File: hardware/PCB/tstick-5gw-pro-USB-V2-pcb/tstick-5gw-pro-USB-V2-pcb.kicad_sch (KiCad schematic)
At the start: 66 parts, among them J1 USB_C_Receptacle_USB2.0, Q1 BSS138, Q2 BSS138, Q3 BSS138, SW1 B3U-1000P, SW2 B3U-1000P, U1 USBLC6-2P6, U2 MCP73871, U3 NCP167AMX330TBG, U4 NCP167AMX180TBG

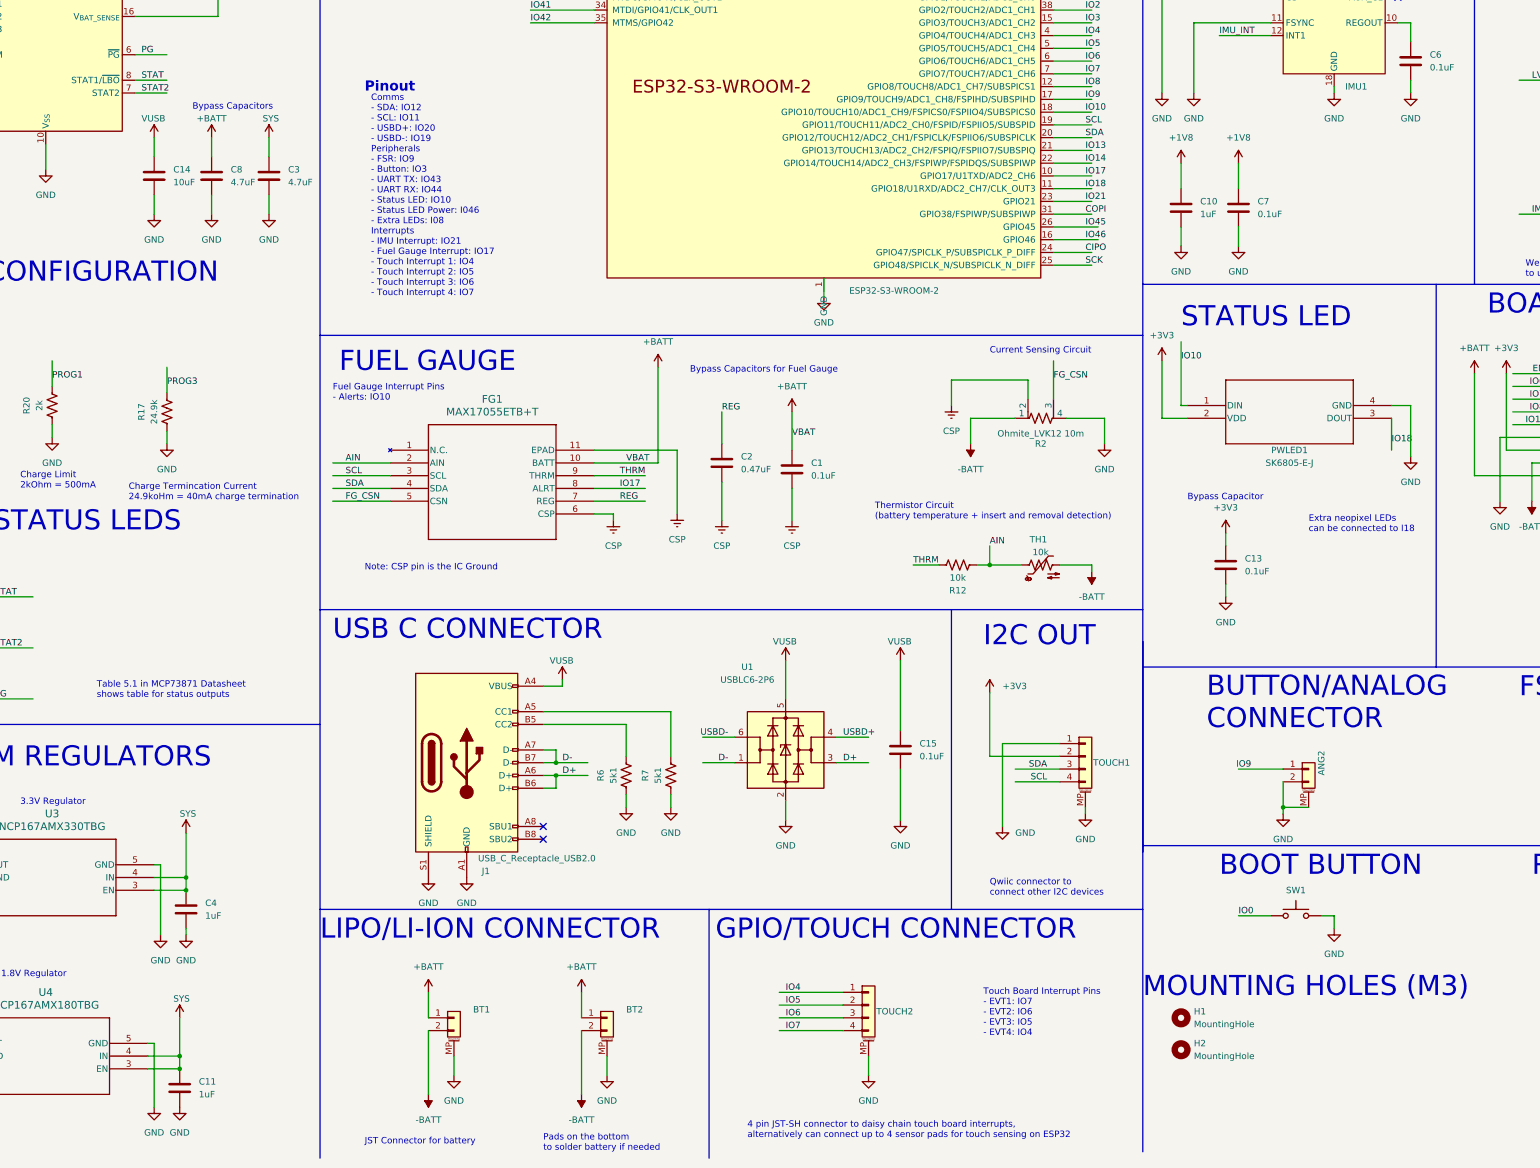
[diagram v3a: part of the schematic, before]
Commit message: removed neopixel, changed BOM, added simple status LEDs
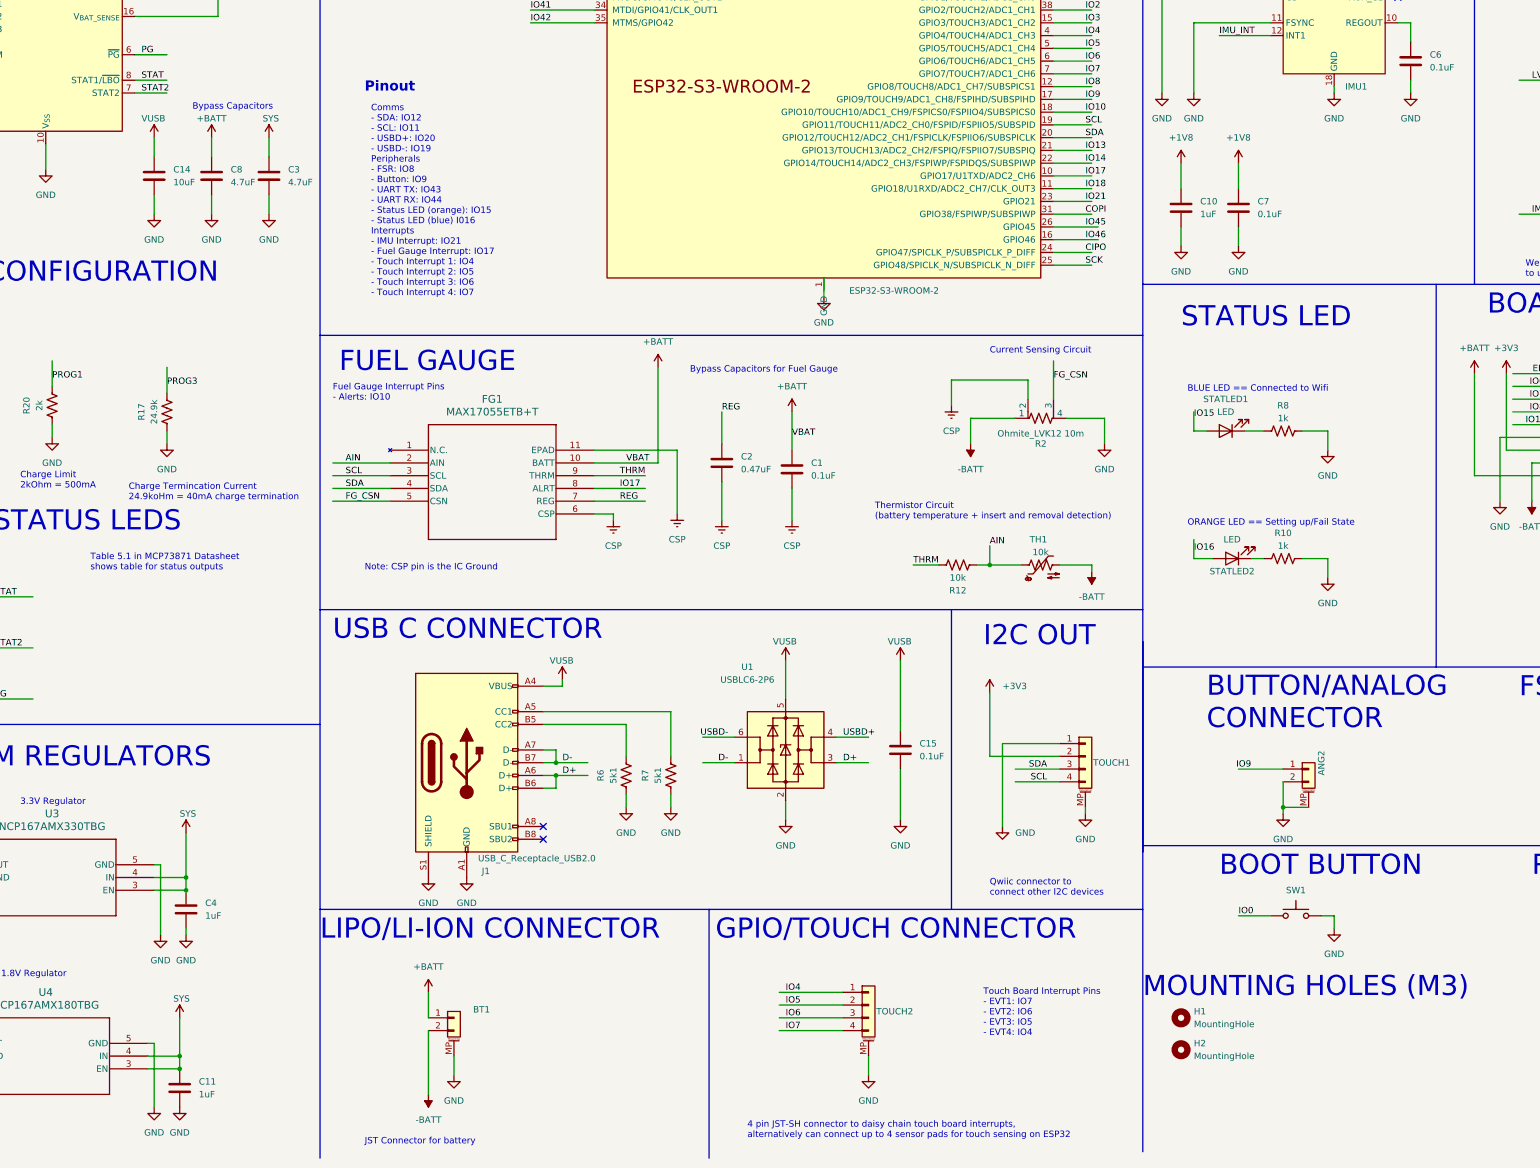
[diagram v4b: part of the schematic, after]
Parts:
- removed BT2: JST-PH-1x02-2.000mm, Connector_JST:JST_PH_B2B-PH-SM4-TB_1x02-1MP_P2.00mm_Vertical, symbol Connector_Generic_MountingPin:Conn_01x02_MountingPin
- removed C13: 0.1uF, Capacitor_SMD:C_0201_0603Metric, symbol Device:C
- removed PWLED1: SK6805-E-J, neopixel-1515-footprints:4492_ADA, symbol neopixel-1515:4492
- added R10, R8: 1k, Resistor_SMD:R_0201_0603Metric, symbol Device:R_US
- added STATLED1, STATLED2: LED, LED_SMD:LED_0402_1005Metric, symbol Device:LED
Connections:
- net GND: now also R10.2, R8.2
- net IO15: now also STATLED1.2 (A)
- net IO16: now also STATLED2.2 (A)
- new net: R8.1, STATLED1.1 (K)
- new net: R10.1, STATLED2.1 (K)
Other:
- note added: "BLUE LED == Connected to Wifi"
- note added: "Comms - SDA: IO12 - SCL: IO11 - USBD+: IO20 - USBD-: IO19 Peripherals - FSR: IO8 - Button: IO9 - UART TX: IO43 - UART RX: IO44 - Status LED (orange): IO15 - Status LED (blue) I016 Interrupts - IMU Interrupt: IO21 - Fuel Gauge Interrupt: IO17 - Touch Interrupt 1: IO4 - Touch Interrupt 2: IO5 - Touch Interrupt 3: IO6 - Touch Interrupt 4: IO7"
- note added: "ORANGE LED == Setting up/Fail State"
- note removed: "Bypass Capacitor"
- note removed: "Comms - SDA: IO12 - SCL: IO11 - USBD+: IO20 - USBD-: IO19 Peripherals - FSR: IO9 - Button: IO3 - UART TX: IO43 - UART RX: IO44 - Status LED: IO10 - Status LED Power: I046 - Extra LEDs: I08 Interrupts - IMU Interrupt: IO21 - Fuel Gauge Interrupt: IO17 - Touch Interrupt 1: IO4 - Touch Interrupt 2: IO5 - Touch Interrupt 3: IO6 - Touch Interrupt 4: IO7"
- note removed: "Extra neopixel LEDs can be connected to I18"
- note removed: "Pads on the bottom to solder battery if needed"

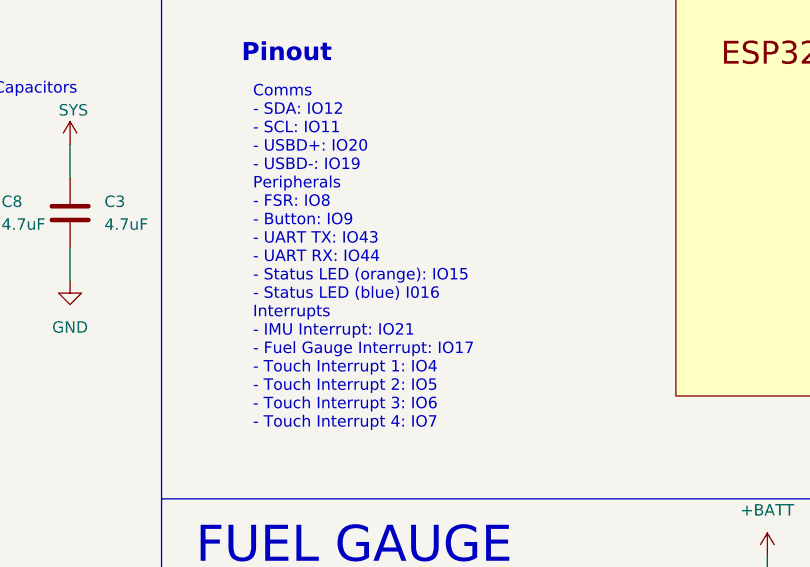
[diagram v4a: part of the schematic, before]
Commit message: Only sends OSC over 1 IP address by default, added class for accessing touch data from custom touch board, uses similar syntax to trill touch class
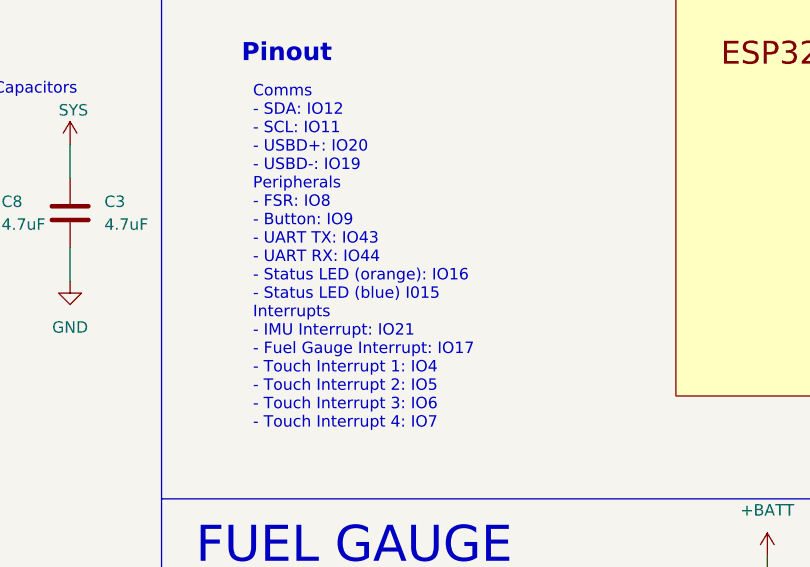
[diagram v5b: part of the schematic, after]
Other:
- note added: "Comms - SDA: IO12 - SCL: IO11 - USBD+: IO20 - USBD-: IO19 Peripherals - FSR: IO8 - Button: IO9 - UART TX: IO43 - UART RX: IO44 - Status LED (orange): IO16 - Status LED (blue) I015 Interrupts - IMU Interrupt: IO21 - Fuel Gauge Interrupt: IO17 - Touch Interrupt 1: IO4 - Touch Interrupt 2: IO5 - Touch Interrupt 3: IO6 - Touch Interrupt 4: IO7"
- note removed: "Comms - SDA: IO12 - SCL: IO11 - USBD+: IO20 - USBD-: IO19 Peripherals - FSR: IO8 - Button: IO9 - UART TX: IO43 - UART RX: IO44 - Status LED (orange): IO15 - Status LED (blue) I016 Interrupts - IMU Interrupt: IO21 - Fuel Gauge Interrupt: IO17 - Touch Interrupt 1: IO4 - Touch Interrupt 2: IO5 - Touch Interrupt 3: IO6 - Touch Interrupt 4: IO7"
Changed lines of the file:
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@@
     (effects (font (size 1.27 1.27)) (justify left bottom))
   )
-  (text "Comms\n- SDA: IO12\n- SCL: IO11\n- USBD+: IO20\n- USBD-: IO19\nPeripherals\n- FSR: IO8\n- Button: IO9\n- UART TX: IO43\n- UART RX: IO44\n- Status LED (orange): IO15\n- Status LED (blue) I016\nInterrupts\n- IMU Interrupt: IO21\n- Fuel Gauge Interrupt: IO17\n- Touch Interrupt 1: IO4\n- Touch Interrupt 2: IO5\n- Touch Interrupt 3: IO6\n- Touch Interrupt 4: IO7"
+  (text "Comms\n- SDA: IO12\n- SCL: IO11\n- USBD+: IO20\n- USBD-: IO19\nPeripherals\n- FSR: IO8\n- Button: IO9\n- UART TX: IO43\n- UART RX: IO44\n- Status LED (orange): IO16\n- Status LED (blue) I015\nInterrupts\n- IMU Interrupt: IO21\n- Fuel Gauge Interrupt: IO17\n- Touch Interrupt 1: IO4\n- Touch Interrupt 2: IO5\n- Touch Interrupt 3: IO6\n- Touch Interrupt 4: IO7"
     (at 120.65 113.03 0)
     (effects (font (size 1.27 1.27)) (justify left bottom))

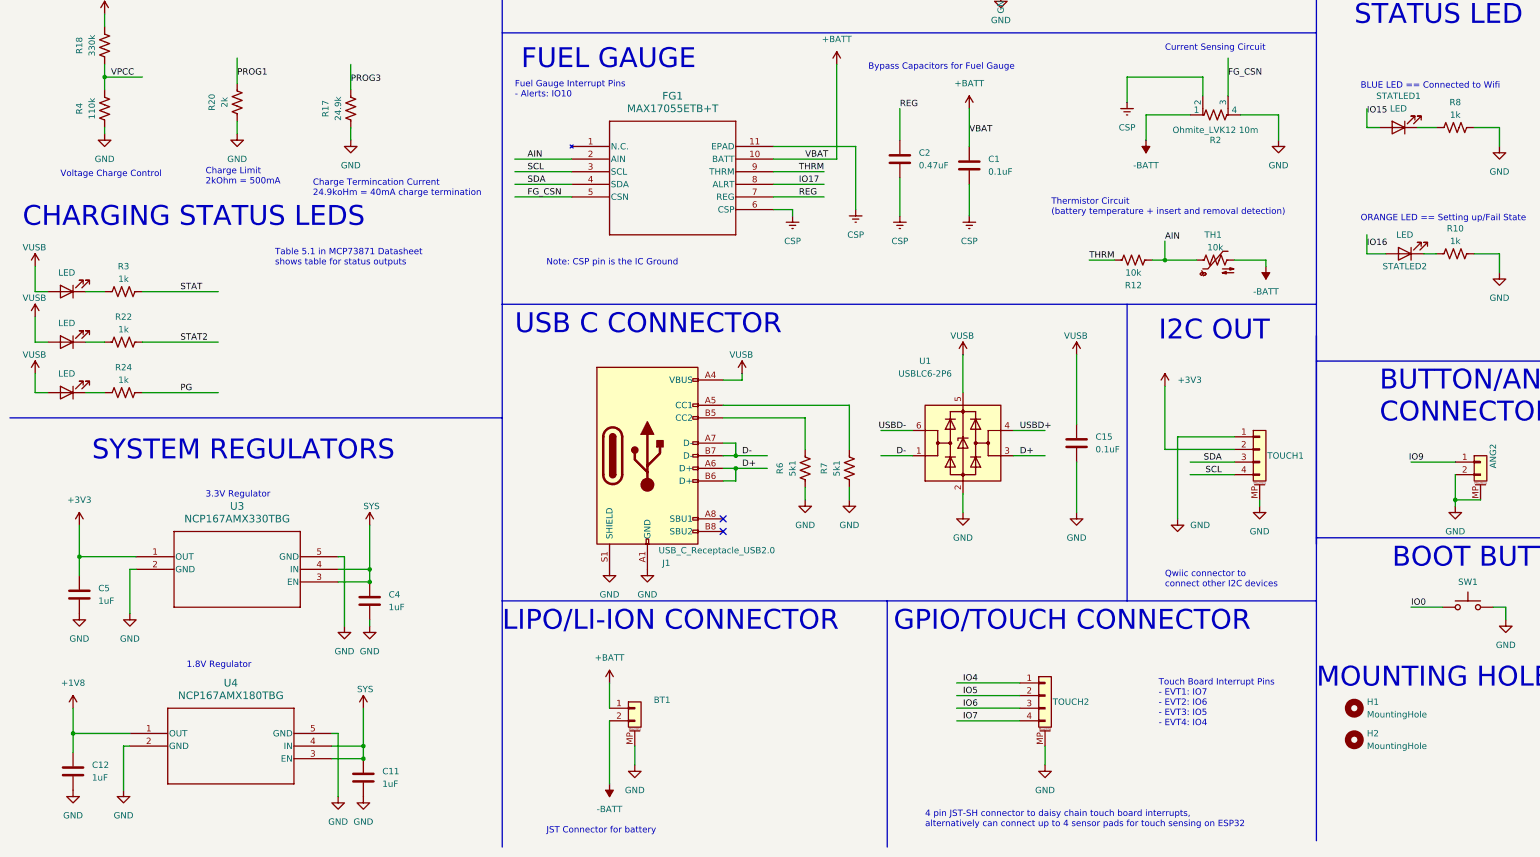
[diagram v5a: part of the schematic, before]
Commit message: removed unused fuel gauge thresholds, added jab thresholds
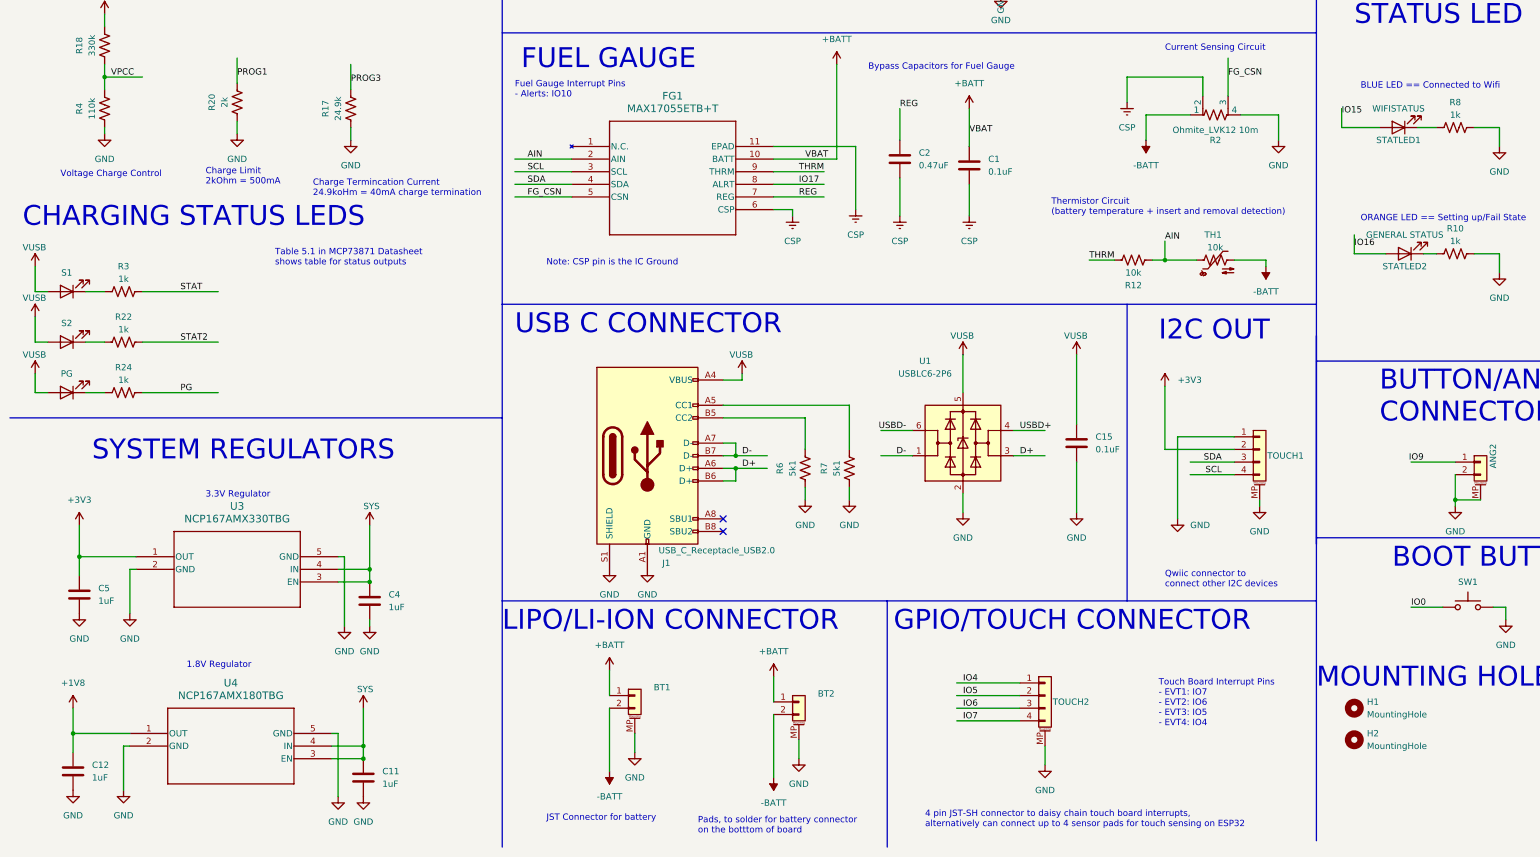
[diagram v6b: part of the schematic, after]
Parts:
- added BT2: JST-PH-1x02-2.000mm, Connector_JST:JST_PH_B2B-PH-SM4-TB_1x02-1MP_P2.00mm_Vertical, symbol Connector_Generic_MountingPin:Conn_01x02_MountingPin
- CHARGLED1: value LED -> S1
- CHARGLED2: value LED -> S2; Description Value Pkg Red 630nm LED Indication - Discrete 1.95V 0402 (1005 Metric) -> Yellow 590nm LED Indication - Discrete 2V 0402 (1005 Metric); Mfg Part # APHHS1005SURCK -> APHHS1005SYCK
- CHARGLED3: value LED -> PG; Description Value Pkg Red 630nm LED Indication - Discrete 1.95V 0402 (1005 Metric) -> Green 570nm LED Indication - Discrete 2.1V 0402 (1005 Metri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; Mfg Part # APHHS1005SURCK -> APHHS1005CGCK
- STATLED1: value LED -> WIFISTATUS
- STATLED2: value LED -> GENERAL STATUS
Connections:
- net +BATT: now also BT2.1 (Pin_1)
- net -BATT: now also BT2.2 (Pin_2)
- net GND: now also BT2.MP (MountPin)
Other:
- note added: "Pads, to solder for battery connector on the botttom of board"
- moved on the sheet: BT1
